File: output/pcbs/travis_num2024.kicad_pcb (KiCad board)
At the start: 2 copper layers, 85.2 x 132.8 mm, 78 parts

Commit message: license
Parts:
- moved LOGO2 20.0 mm to (90.1, 110.2)
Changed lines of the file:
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@@
     )
   )
-      (gr_text "JLCJLCJLCJLC"
-        (at 70.075 115.24999999999997 0)
-        (layer F.SilkS)
-        (effects
-          (font
-            (size 1 1)
-            (thickness 0.15)
-            )
-          )
-      )
-      (gr_text "JLCJLCJLCJLC"
-        (at 70.075 115.24999999999997 0)
-        (layer B.SilkS)
-        (effects
-          (font
-            (size 1 1)
-            (thickness 0.15)
-            )
-            (justify  mirror)
-          )
-      )
       (module "ceoloide:ergogen_logo" (layer "F.Cu")
-        (at 70.075 110.24999999999997 0)
+        (at 70.07499999999999 110.24999999999997 0)
         (attr virtual)
         (fp_text reference "LOGO1" (at 9.144 0 0) (layer "F.Fab") hide
@@
       )
     (module "travis:travis" (layer "F.Cu")
-    (at 70.075 110.24999999999997 0)
+    (at 90.125 110.24999999999997 0)
     (attr virtual)
     (fp_text reference "LOGO2" (at 0 -0.5 0)(layer "F.SilkS") hide
@@
    )
       (gr_text "2024.04.07"
-        (at 70.075 108.49999999999997 0)
+        (at 90.125 108.49999999999997 0)
         (layer F.SilkS)
         (effects
@@
           )
       )
+      (gr_text "JLCJLCJLCJLC"
+        (at 90.125 115.24999999999997 0)
+        (layer F.SilkS)
+        (effects
+          (font
+            (size 1 1)
+            (thickness 0.15)
+            )
+          )
+      )
+      (gr_text "JLCJLCJLCJLC"
+        (at 90.125 115.24999999999997 0)
+        (layer B.SilkS)
+        (effects
+          (font
+            (size 1 1)
+            (thickness 0.15)
+            )
+            (justify  mirror)
+          )
+      )

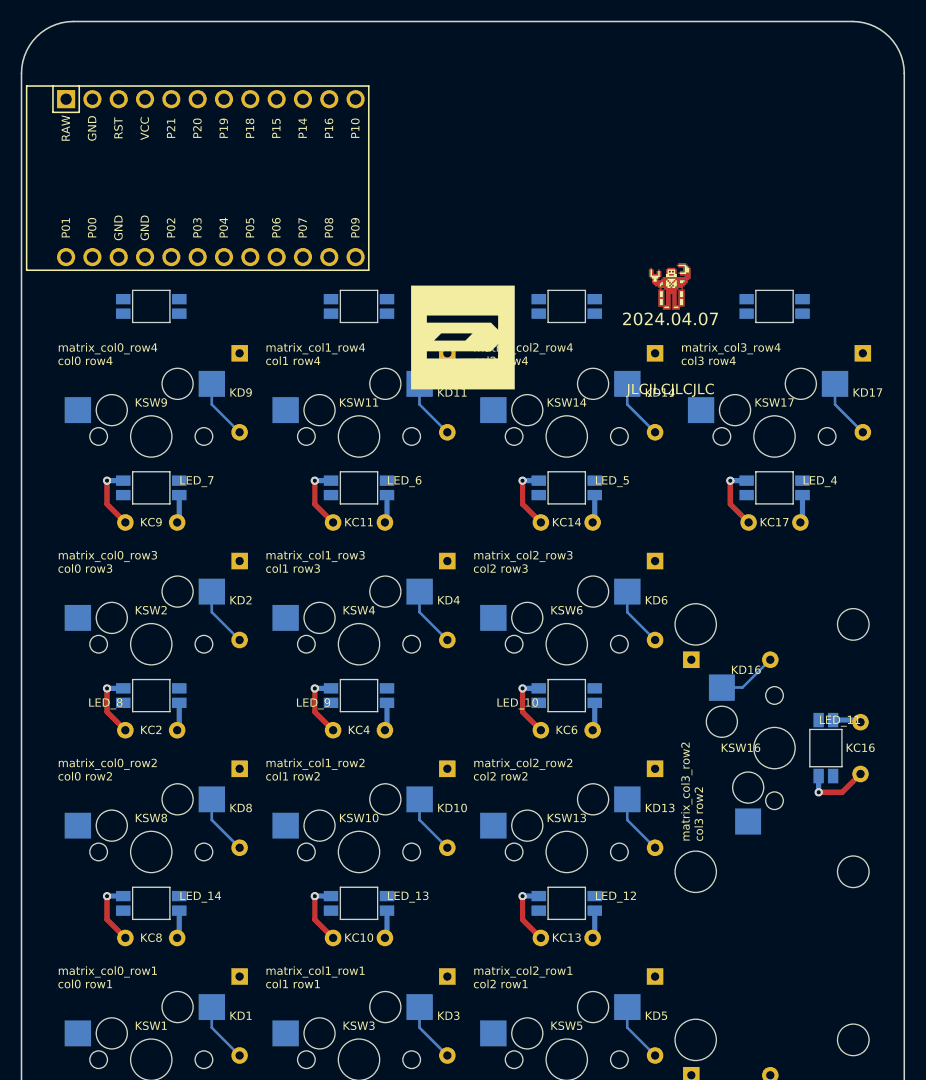
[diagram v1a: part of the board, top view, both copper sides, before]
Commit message: numpad basic layout
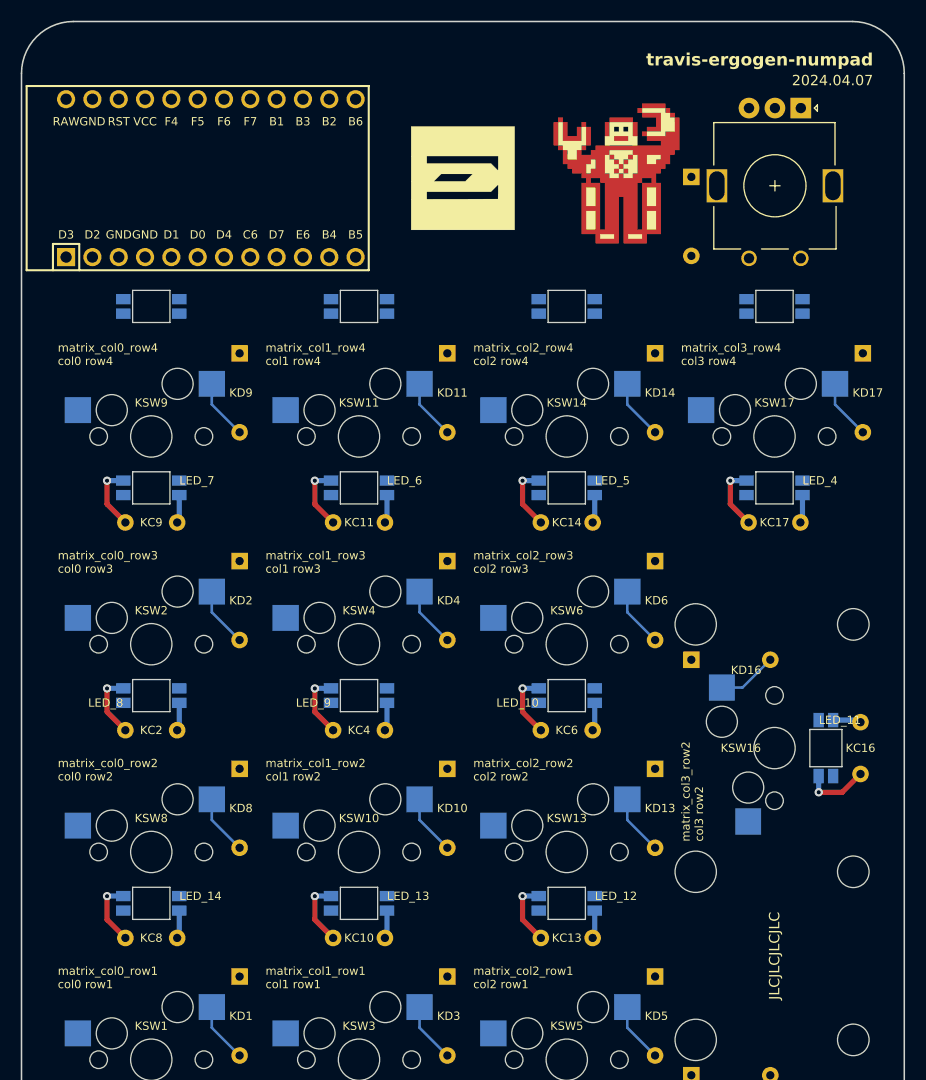
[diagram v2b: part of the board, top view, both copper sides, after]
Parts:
- added D1: 1N4148, ScottoKeebs_Components:Diode_DO-35, B.Cu at (92.1, 94.7)
- added ROT1: EC11, travis:ec11, F.Cu at (100.2, 95.7)
- MCU1: value (none) -> Arduino Pro Micro; footprint ProMicro -> Arduino_Pro_Micro
- moved LOGO2 16.2 mm to (85.1, 94.9)
- moved LOGO1 15.4 mm to (70.1, 94.9)
- turned MCU1 to 90 degrees
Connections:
- net P10 renamed LED
- net P14 renamed scrA
- net P15 renamed scrC
- net P16 renamed B4
- net P18 renamed mux0
- net P19 renamed mux1
- net P20 renamed mux2
- net P21 renamed mux3
- MCU1 pad 1: RAW -> D3
- MCU1 pad 13: P1 -> encC
- MCU1 pad 14: P0 -> encA
- MCU1 pad 15: GND -> row5
- MCU1 pad 16: GND -> row4
- MCU1 pad 17: P2 -> row3
- MCU1 pad 18: P3 -> row2
- MCU1 pad 19: P4 -> row1
- MCU1 pad 2: GND -> D2
- MCU1 pad 20: P5 -> row0
- MCU1 pad 21: P6 -> VCC
- MCU1 pad 22: P7 -> RST
- MCU1 pad 23: P8 -> GND
- MCU1 pad 24: P9 -> RAW
- MCU1 pad 3: RST -> GND
- MCU1 pad 4: VCC -> GND
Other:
- board text added: "travis-ergogen-numpad"

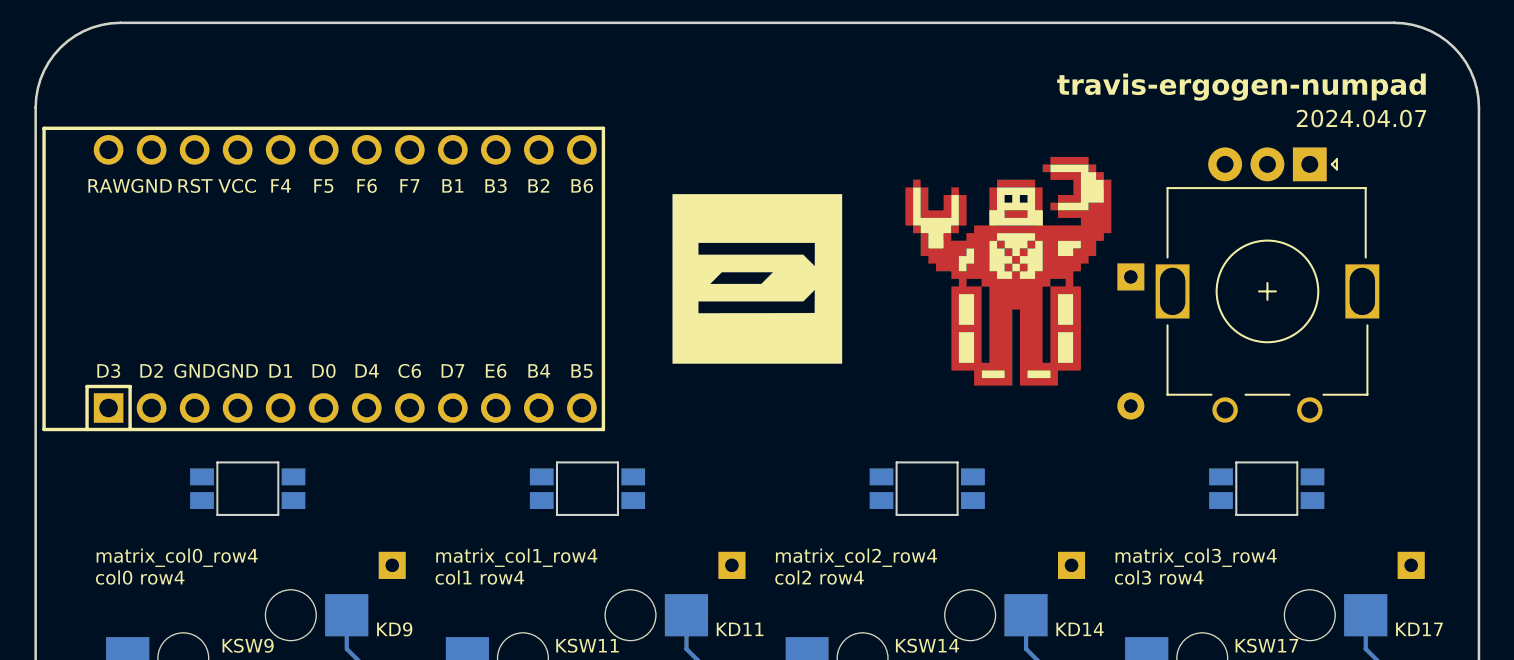
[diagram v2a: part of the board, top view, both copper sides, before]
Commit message: layout and label fixes
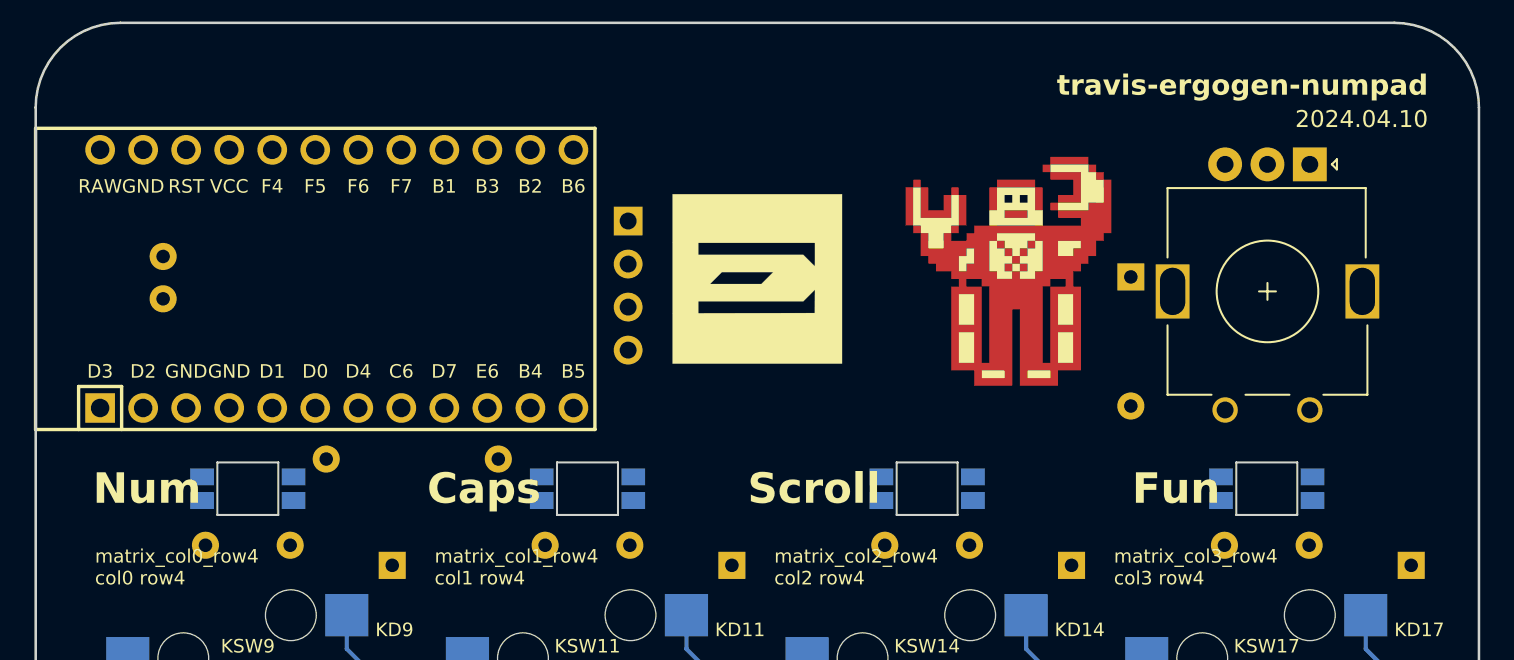
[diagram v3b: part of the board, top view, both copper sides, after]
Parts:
- added C1: 6.3V 1000uF, Capacitor_THT:C_Radial_D6.3mm_H11.0mm_P2.50mm, B.Cu at (35.0, 93.5)
- added C2: 104, Capacitor_THT:C_Disc_D4.7mm_W2.5mm_P5.00mm, B.Cu at (42.5, 110.6)
- added C3: 104, Capacitor_THT:C_Disc_D4.7mm_W2.5mm_P5.00mm, B.Cu at (62.5, 110.6)
- added C4: 104, Capacitor_THT:C_Disc_D4.7mm_W2.5mm_P5.00mm, B.Cu at (82.6, 110.6)
- added C5: 104, Capacitor_THT:C_Disc_D4.7mm_W2.5mm_P5.00mm, B.Cu at (102.7, 110.6)
- added OLED1: OLED, lib:OLED_headers, F.Cu at (64.0, 101.2)
- added R1: 470R, Resistor_THT:R_Axial_DIN0207_L6.3mm_D2.5mm_P10.16mm_Horizontal, B.Cu at (54.8, 105.5)
- LED1, LED2, LED3, LED4: value (none) -> SK6812mini-e; footprint ceoloide:led_SK6812mini-e (per-keysingle-side) -> travis:led_SK6812mini-e (per-key, single-side)
- moved MCU1 0.50 mm to (45.2, 94.9)
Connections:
- D1 pad 1: row5 -> row4
- MCU1 pad 10: scrA -> row3
- MCU1 pad 11: B4 -> row4
- MCU1 pad 15: row5 -> B3
- MCU1 pad 16: row4 -> B1
- MCU1 pad 17: row3 -> col3
- MCU1 pad 18: row2 -> col2
- MCU1 pad 19: row1 -> col1
- MCU1 pad 20: row0 -> col0
- MCU1 pad 5: mux3 -> sda
- MCU1 pad 6: mux2 -> scl
- MCU1 pad 7: mux1 -> row0
- MCU1 pad 8: mux0 -> row1
- MCU1 pad 9: scrC -> row2
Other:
- board text added: "2024.04.10"
- board text added: "Caps"
- board text added: "Fun"
- board text added: "LED_0"
- board text added: "LED_1"
- board text added: "LED_2"
- board text added: "LED_3"
- board text added: "Num"
- board text added: "Scroll"
- board text removed: "2024.04.07"

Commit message: roc logo on back
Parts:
- added ROC1: , travis:travis, B.Cu at (70.1, 94.9)

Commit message: holes, roc text
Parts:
- added HOLE1: , travis:MountingHole_2.2mm_M2_Pad_Via, F.Cu at (31.0, 83.2)
- added HOLE2: , travis:MountingHole_2.2mm_M2_Pad_Via, F.Cu at (109.2, 83.2)
- added HOLE3: , travis:MountingHole_2.2mm_M2_Pad_Via, F.Cu at (109.2, 209.0)
- added HOLE4: , travis:MountingHole_2.2mm_M2_Pad_Via, F.Cu at (31.0, 209.0)
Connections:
- C2 pad 1: VCC -> RAW
- C3 pad 1: VCC -> RAW
- C4 pad 1: VCC -> RAW
- C5 pad 1: VCC -> RAW
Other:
- board text added: "made with ♥ in #ROC"

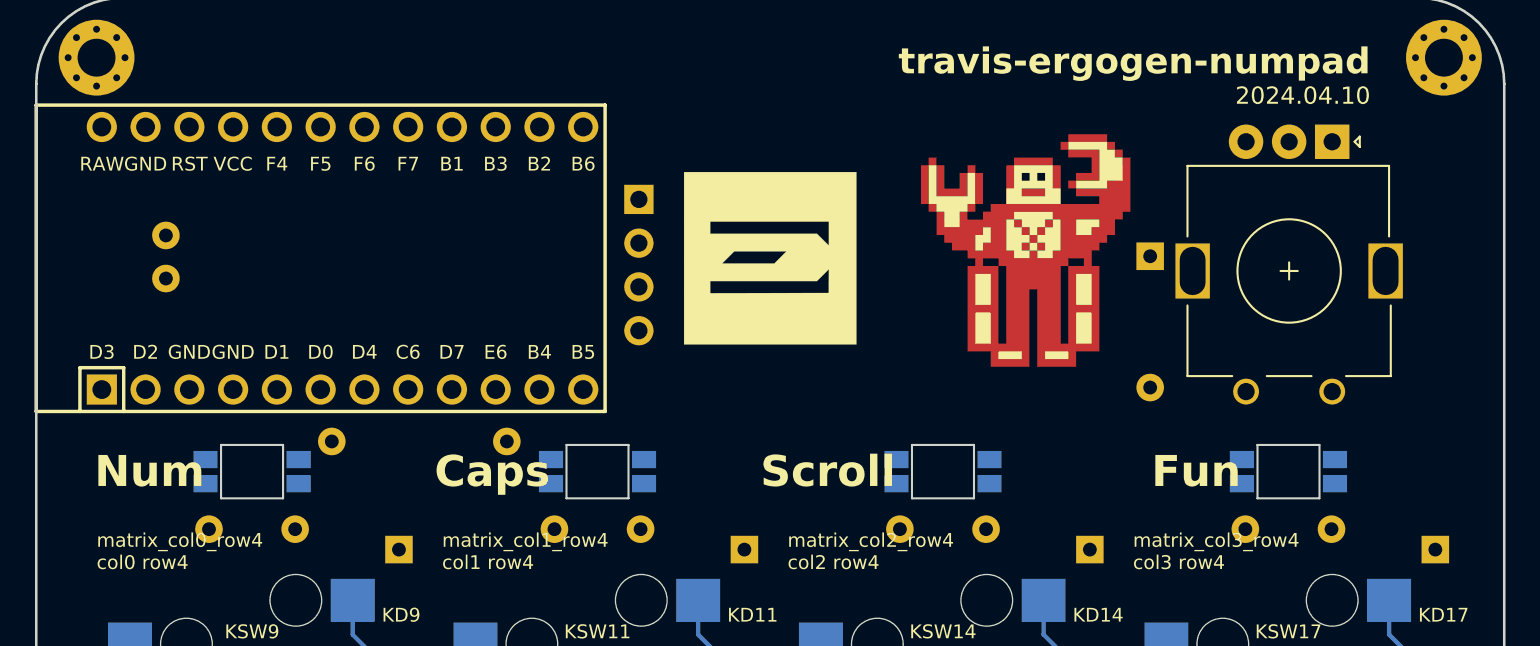
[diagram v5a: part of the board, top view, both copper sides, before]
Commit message: text and cap fixes
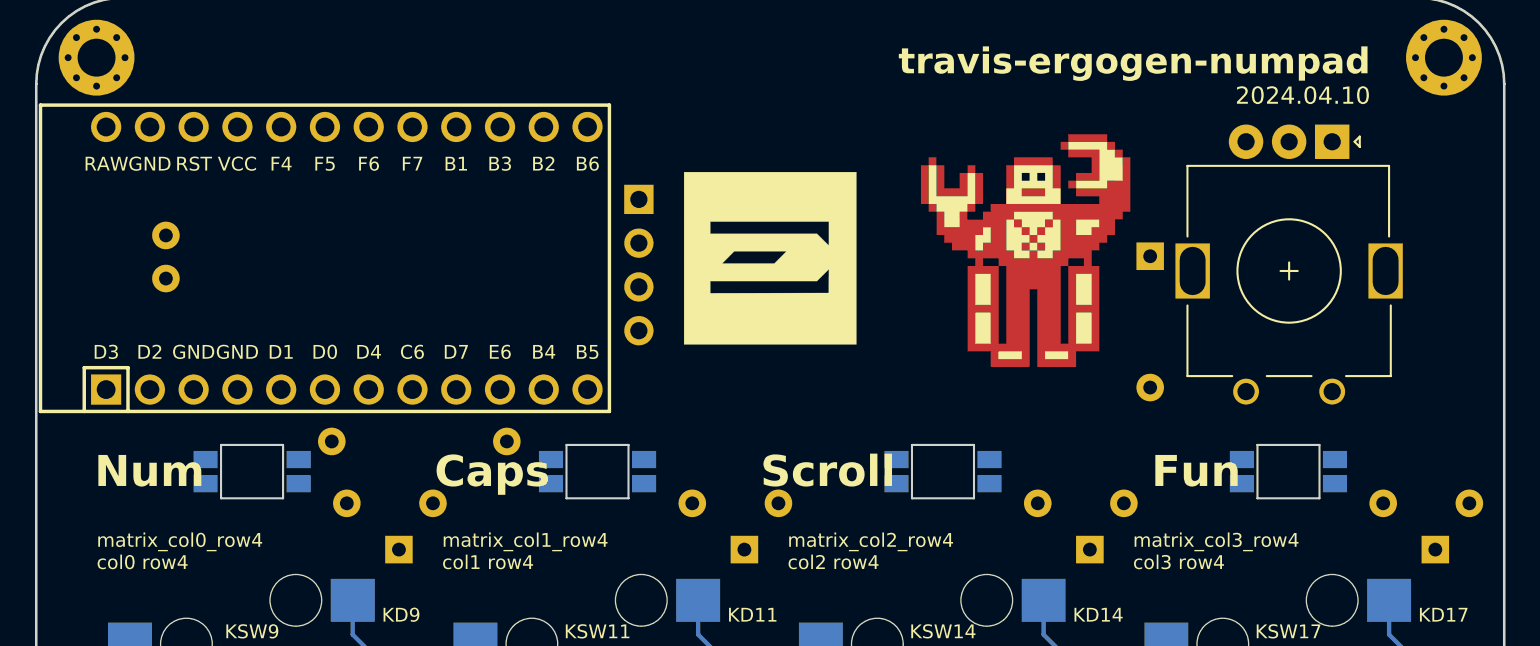
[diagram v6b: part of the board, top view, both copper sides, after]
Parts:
- moved C2 3.35 mm to (45.5, 109.1), turned to 0 degrees
- moved C3 3.35 mm to (65.5, 109.1), turned to 0 degrees
- moved C4 3.35 mm to (85.6, 109.1), turned to 0 degrees
- moved C5 3.35 mm to (105.7, 109.1), turned to 0 degrees
- moved MCU1 0.25 mm to (45.5, 94.9)
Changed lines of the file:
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@@
     (module "Arduino_Pro_Micro"
     (layer "F.Cu")
-    (at 45.25 94.86749999999998 90)
+    (at 45.5 94.86749999999998 90)
     (attr through_hole)
     (fp_text reference "MCU1" (at 0 1.625 90) (layer "F.SilkS") hide
@@
     (descr "C, Disc series, Radial, pin pitch=5.00mm, , diameter*width=4.7*2.5mm^2, Capacitor, http://www.vishay.com/docs/45233/krseries.pdf")
     (tags "C Disc series Radial pin pitch 5.00mm  diameter 4.7mm width 2.5mm Capacitor")
-    (at 42.5 110.58999999999997 180)
-    (fp_text reference "C2" (at 7.5 0 180) (layer B.SilkS) hide
+    (at 45.5 109.08999999999997 0)
+    (fp_text reference "C2" (at 7.5 0 0) (layer B.SilkS) hide
       (effects (font (size 1 1) (thickness 0.15)) (justify mirror))
     )
-    (fp_text value "104" (at -2.5 0 180) (layer B.Fab)
+    (fp_text value "104" (at -2.5 0 0) (layer B.Fab)
       (effects (font (size 1 1) (thickness 0.15)))
     )
@@
     (descr "C, Disc series, Radial, pin pitch=5.00mm, , diameter*width=4.7*2.5mm^2, Capacitor, http://www.vishay.com/docs/45233/krseries.pdf")
     (tags "C Disc series Radial pin pitch 5.00mm  diameter 4.7mm width 2.5mm Capacitor")
-    (at 62.55 110.58999999999997 180)
-    (fp_text reference "C3" (at 7.5 0 180) (layer B.SilkS) hide
+    (at 65.55 109.08999999999997 0)
+    (fp_text reference "C3" (at 7.5 0 0) (layer B.SilkS) hide
       (effects (font (size 1 1) (thickness 0.15)) (justify mirror))
     )
-    (fp_text value "104" (at -2.5 0 180) (layer B.Fab)
+    (fp_text value "104" (at -2.5 0 0) (layer B.Fab)
       (effects (font (size 1 1) (thickness 0.15)))
     )
@@
     (descr "C, Disc series, Radial, pin pitch=5.00mm, , diameter*width=4.7*2.5mm^2, Capacitor, http://www.vishay.com/docs/45233/krseries.pdf")
     (tags "C Disc series Radial pin pitch 5.00mm  diameter 4.7mm width 2.5mm Capacitor")
-    (at 82.6 110.58999999999997 180)
-    (fp_text reference "C4" (at 7.5 0 180) (layer B.SilkS) hide
+    (at 85.6 109.08999999999997 0)
+    (fp_text reference "C4" (at 7.5 0 0) (layer B.SilkS) hide
       (effects (font (size 1 1) (thickness 0.15)) (justify mirror))
     )
-    (fp_text value "104" (at -2.5 0 180) (layer B.Fab)
+    (fp_text value "104" (at -2.5 0 0) (layer B.Fab)
       (effects (font (size 1 1) (thickness 0.15)))
     )
@@
     (descr "C, Disc series, Radial, pin pitch=5.00mm, , diameter*width=4.7*2.5mm^2, Capacitor, http://www.vishay.com/docs/45233/krseries.pdf")
     (tags "C Disc series Radial pin pitch 5.00mm  diameter 4.7mm width 2.5mm Capacitor")
-    (at 102.65 110.58999999999997 180)
-    (fp_text reference "C5" (at 7.5 0 180) (layer B.SilkS) hide
+    (at 105.65 109.08999999999997 0)
+    (fp_text reference "C5" (at 7.5 0 0) (layer B.SilkS) hide
       (effects (font (size 1 1) (thickness 0.15)) (justify mirror))
     )
-    (fp_text value "104" (at -2.5 0 180) (layer B.Fab)
+    (fp_text value "104" (at -2.5 0 0) (layer B.Fab)
       (effects (font (size 1 1) (thickness 0.15)))
     )
@@
         (layer F.SilkS)
         (effects
-          (font (face "CaskaydiaMono NFP")
+          (font (face "MesloLGM Nerd Font")
             (size 1.8 1.8)
             (thickness 0.15)
@@
         (layer F.SilkS)
         (effects
-          (font (face "CaskaydiaMono NFP")
+          (font (face "MesloLGM Nerd Font")
             (size 1.8 1.8)
             (thickness 0.15)
@@
         (layer F.SilkS)
         (effects
-          (font (face "CaskaydiaMono NFP")
+          (font (face "MesloLGM Nerd Font")
             (size 1.8 1.8)
             (thickness 0.15)
@@
         (layer F.SilkS)
         (effects
-          (font (face "CaskaydiaMono NFP")
+          (font (face "MesloLGM Nerd Font")
             (size 1.8 1.8)
             (thickness 0.15)
@@
         (layer B.SilkS)
         (effects
-          (font (face "CaskaydiaMono NFP")
+          (font (face "MesloLGM Nerd Font")
             (size 1 1)
             (thickness 0.15)
@@
         (layer F.SilkS)
         (effects
-          (font (face "CaskaydiaMono NFP")
+          (font (face "MesloLGM Nerd Font")
             (size 1.5 1.5)
             (thickness 0.15)
@@
         (layer F.SilkS)
         (effects
-          (font (face "CaskaydiaMono NFP")
+          (font (face "MesloLGM Nerd Font")
             (size 1 1)
             (thickness 0.15)
